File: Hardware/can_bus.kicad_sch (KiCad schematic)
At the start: 4 parts, among them U14 MCP2542FDxMF

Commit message: sync
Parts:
- renumbered C35 to C27, C36 to C28, FB4 to FB3, U14 to U8
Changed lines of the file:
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@@
 (kicad_sch
-	(version 20231120)
+	(version 20250114)
 	(generator "eeschema")
-	(generator_version "8.0")
+	(generator_version "9.0")
 	(paper "A4")
 	(title_block
@@
 		(comment 1 "Reviewer:")
 	)
+	(text "The IC has internal ESD protection"
+		(exclude_from_sim no)
+		(at 147.32 118.11 0)
+		(effects
+			(font
+				(size 1.27 1.27)
+			)
+			(justify left bottom)
+		)
+	)
+	(text "CAN FD compliant transceiver\n"
+		(exclude_from_sim no)
+		(at 147.32 120.65 0)
+		(effects
+			(font
+				(size 1.27 1.27)
+			)
+			(justify left bottom)
+		)
+	)
 	(junction
 		(at 135.89 81.28)
@@
 		)
 	)
-	(text "The IC has internal ESD protection"
-		(exclude_from_sim no)
-		(at 147.32 118.11 0)
+	(hierarchical_label "CAN_H"
+		(shape bidirectional)
+		(at 154.94 102.87 0)
 		(effects
 			(font
 				(size 1.27 1.27)
 			)
-			(justify left bottom)
-		)
-	)
-	(text "CAN FD compliant transceiver\n"
-		(exclude_from_sim no)
-		(at 147.32 120.65 0)
+			(justify left)
+		)
+	)
+	(hierarchical_label "CAN_RX"
+		(shape output)
+		(at 129.54 102.87 180)
 		(effects
 			(font
 				(size 1.27 1.27)
 			)
-			(justify left bottom)
-		)
-	)
-	(hierarchical_label "CAN_H"
+			(justify right)
+		)
+	)
+	(hierarchical_label "CAN_L"
 		(shape bidirectional)
-		(at 154.94 102.87 0)
-		(fields_autoplaced yes)
+		(at 154.94 107.95 0)
 		(effects
 			(font
@@
 		)
 	)
-	(hierarchical_label "CAN_RX"
-		(shape output)
-		(at 129.54 102.87 180)
-		(fields_autoplaced yes)
+	(hierarchical_label "CAN_TX"
+		(shape input)
+		(at 129.54 100.33 180)
 		(effects
 			(font
@@
 		)
 	)
-	(hierarchical_label "CAN_L"
-		(shape bidirectional)
-		(at 154.94 107.95 0)
-		(fields_autoplaced yes)
-		(effects
-			(font
-				(size 1.27 1.27)
-			)
-			(justify left)
-		)
-	)
-	(hierarchical_label "CAN_TX"
-		(shape input)
-		(at 129.54 100.33 180)
-		(fields_autoplaced yes)
-		(effects
-			(font
-				(size 1.27 1.27)
-			)
-			(justify right)
-		)
-	)
 	(symbol
 		(lib_id "Device:C_Small")
@@
 		(dnp no)
 		(fields_autoplaced yes)
-		(property "Reference" "C36"
+		(property "Reference" "C28"
 			(at 148.59 84.4613 0)
 			(effects
@@
 		(on_board yes)
 		(dnp no)
-		(property "Reference" "#PWR0109"
+		(property "Reference" "#PWR061"
 			(at 133.35 95.25 0)
 			(effects
@@
 		(on_board yes)
 		(dnp no)
-		(property "Reference" "#PWR0112"
+		(property "Reference" "#PWR064"
 			(at 142.24 123.19 0)
 			(effects
@@
 		(on_board yes)
 		(dnp no)
-		(property "Reference" "#PWR0108"
+		(property "Reference" "#PWR060"
 			(at 128.27 118.11 0)
 			(effects
@@
 		(dnp no)
 		(fields_autoplaced yes)
-		(property "Reference" "#FLG010"
+		(property "Reference" "#FLG09"
 			(at 160.655 88.9 0)
 			(effects
@@
 		(on_board yes)
 		(dnp no)
-		(property "Reference" "#PWR0113"
+		(property "Reference" "#PWR065"
 			(at 146.05 95.25 0)
 			(effects
@@
 		(on_board yes)
 		(dnp no)
-		(property "Reference" "C35"
+		(property "Reference" "C27"
 			(at 130.81 84.4613 0)
 			(effects
@@
 		(dnp no)
 		(fields_autoplaced yes)
-		(property "Reference" "#PWR0110"
+		(property "Reference" "#PWR062"
 			(at 135.89 83.82 0)
 			(effects
@@
 		(on_board yes)
 		(dnp no)
-		(property "Reference" "U14"
+		(property "Reference" "U8"
 			(at 149.86 114.3 0)
 			(effects
@@
 		(dnp no)
 		(fields_autoplaced yes)
-		(property "Reference" "#PWR0111"
+		(property "Reference" "#PWR063"
 			(at 142.24 78.105 0)
 			(effects
@@
 		(dnp no)
 		(fields_autoplaced yes)
-		(property "Reference" "FB4"
+		(property "Reference" "FB3"
 			(at 144.78 76.7969 0)
 			(effects

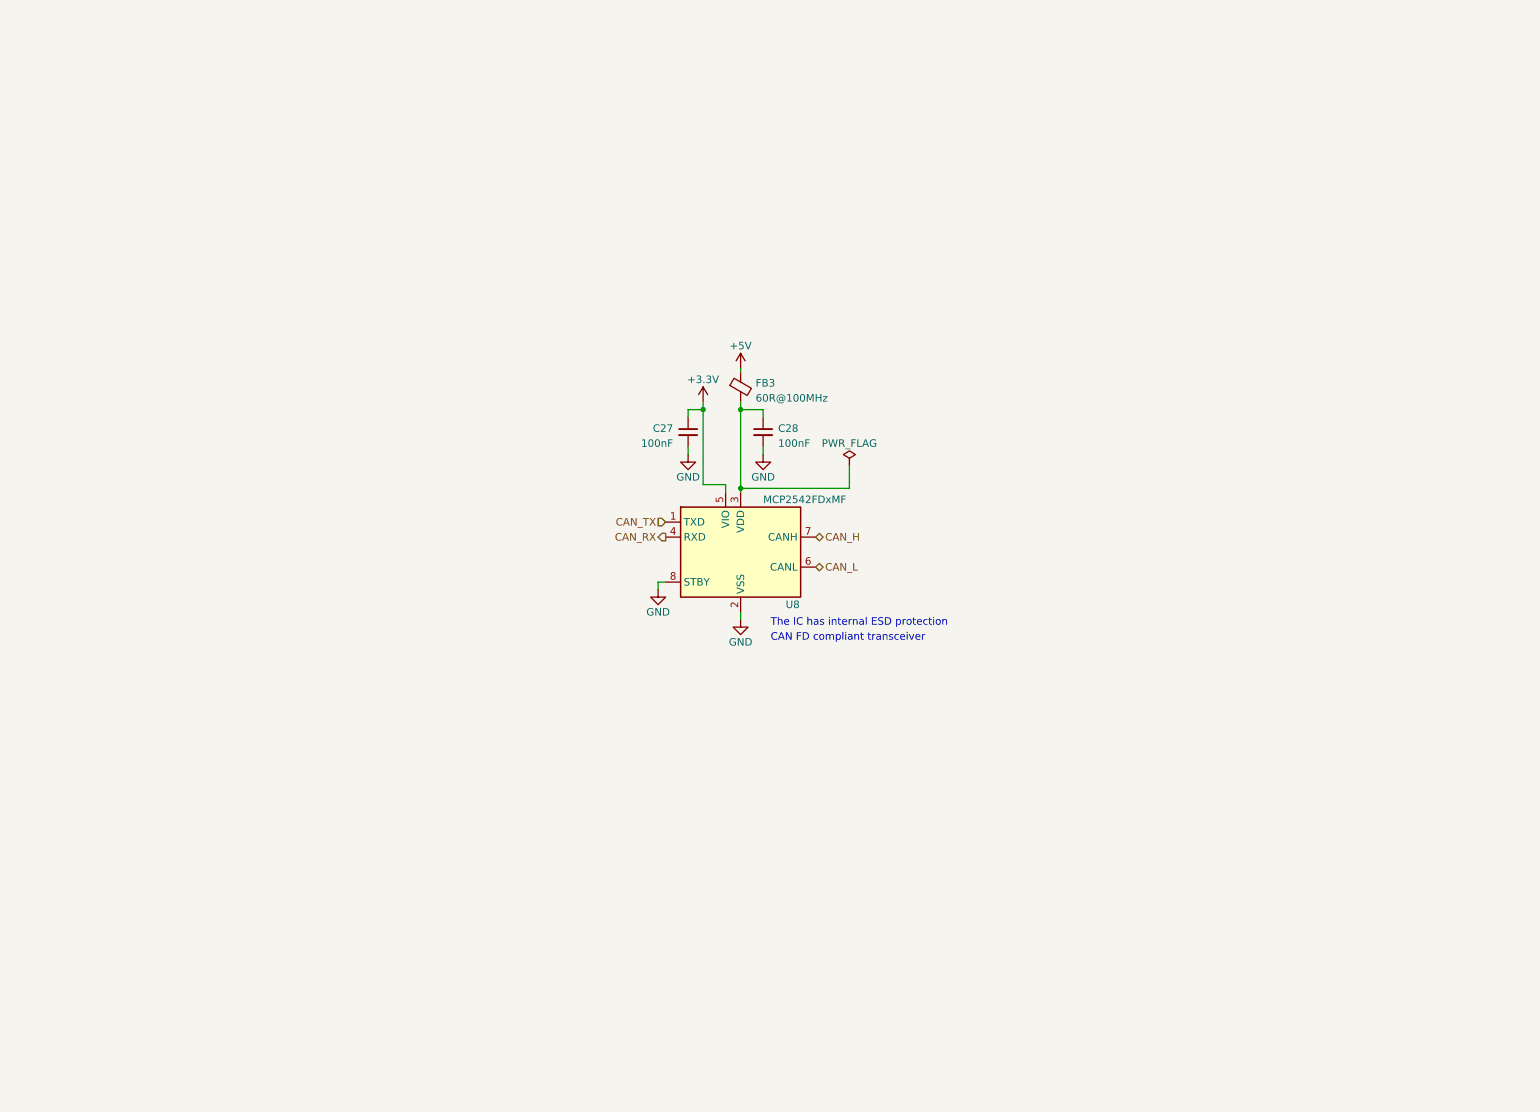
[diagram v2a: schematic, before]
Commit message: Created new hardware version 2.0
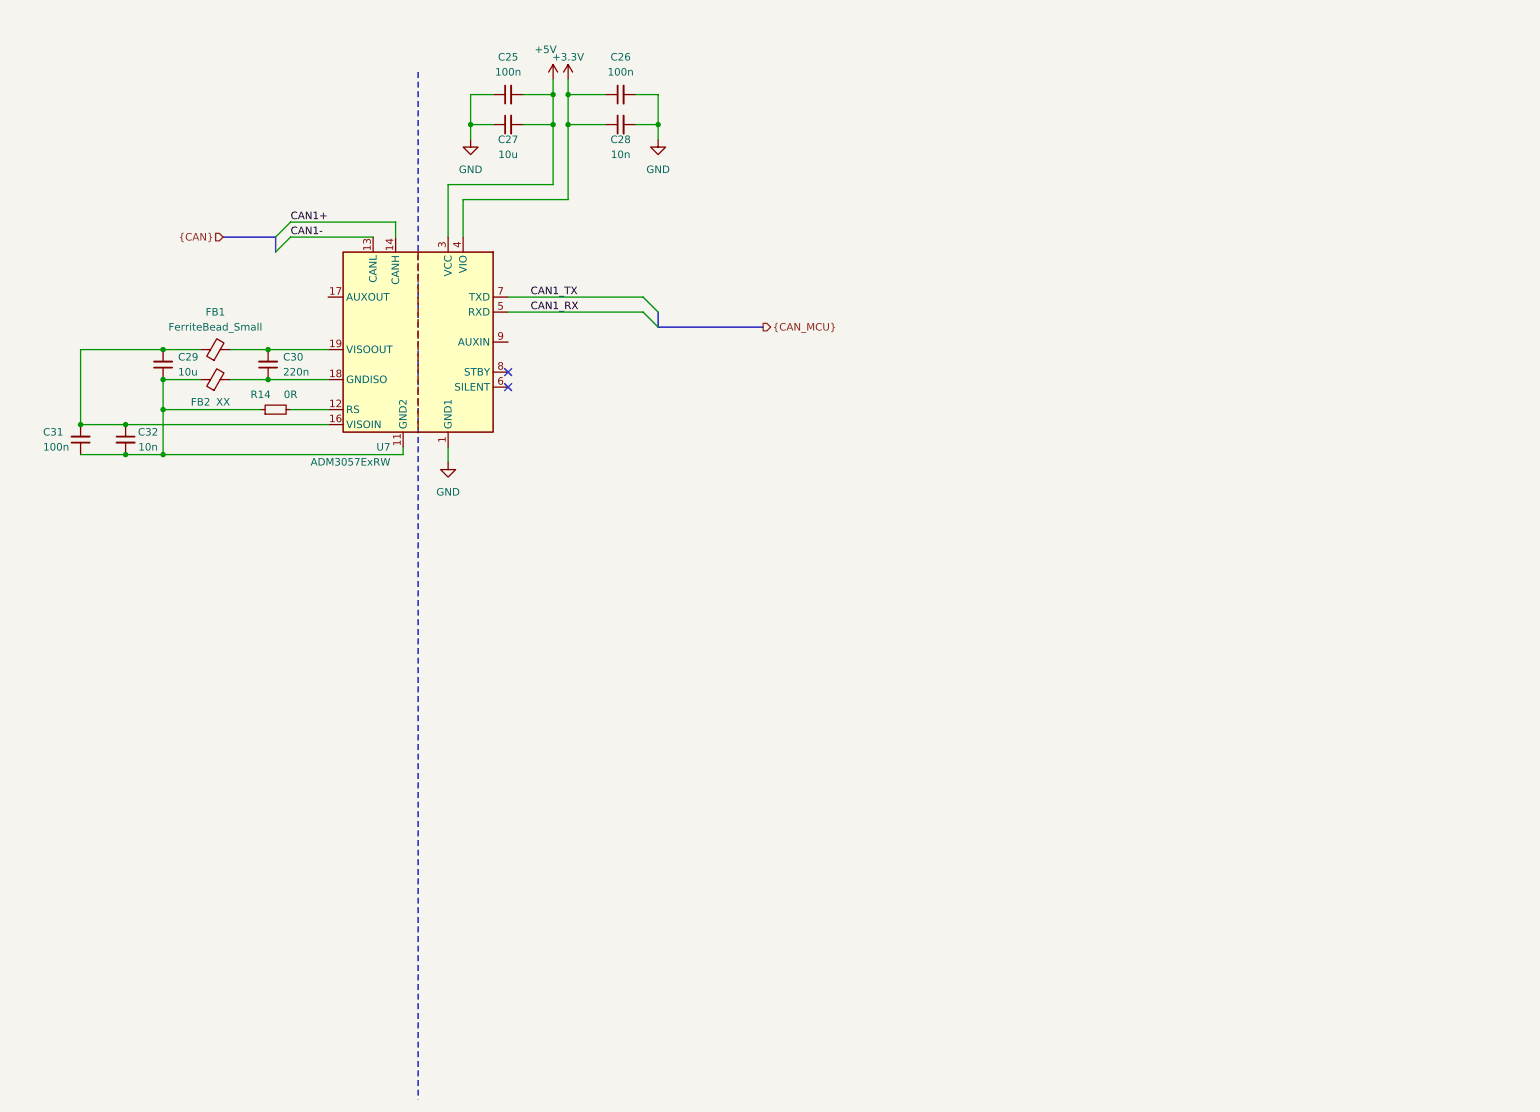
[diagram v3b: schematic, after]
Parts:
- removed FB3: 60R@100MHz, Inductor_SMD:L_0603_1608Metric, symbol Device:FerriteBead_Small
- removed U8: MCP2542FDxMF, Package_DFN_QFN:DFN-8-1EP_3x3mm_P0.65mm_EP1.55x2.4mm, symbol Interface_CAN_LIN:MCP2542FDxMF
- added C25, C26, C31: 100n, Capacitor_SMD:C_0603_1608Metric_Pad1.08x0.95mm_HandSolder, symbol Device:C_Small
- added C29: 10u, Capacitor_SMD:C_0603_1608Metric_Pad1.08x0.95mm_HandSolder, symbol Device:C_Small
- added C30: 220n, Capacitor_SMD:C_0603_1608Metric_Pad1.08x0.95mm_HandSolder, symbol Device:C_Small
- added C32: 10n, Capacitor_SMD:C_0603_1608Metric_Pad1.08x0.95mm_HandSolder, symbol Device:C_Small
- added FB1: FerriteBead_Small, symbol Device:FerriteBead_Small
- added FB2: XX, symbol Device:FerriteBead_Small
- added R14: 0R, Resistor_SMD:R_0603_1608Metric_Pad0.98x0.95mm_HandSolder, symbol Device:R_Small
- added U7: ADM3057ExRW, Package_SO:SOIC-20W_7.5x12.8mm_P1.27mm, symbol Interface_CAN_LIN:ADM3057ExRW
- C27: value 100nF -> 10u; footprint Capacitor_SMD:C_0402_1005Metric_Pad0.74x0.62mm_HandSolder -> Capacitor_SMD:C_0603_1608Metric_Pad1.08x0.95mm_HandSolder
- C28: value 100nF -> 10n; footprint Capacitor_SMD:C_0402_1005Metric_Pad0.74x0.62mm_HandSolder -> Capacitor_SMD:C_0603_1608Metric_Pad1.08x0.95mm_HandSolder
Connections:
- net +3.3V: now also C28.1, C26.1, U7.4 (VIO); no longer C27.1
- net +5V: now also C27.2, C25.2, U7.3 (VCC)
- net GND: now also C27.1, C25.1, C26.2, U7.1 (GND1), U7.10 (GND1), U7.2 (GND1); no longer C27.2
- new net: C29.1, C31.1, C32.2, FB2.1, R14.1, U7.11 (GND2), U7.15 (GND2)
- new net: C30.1, FB2.2, U7.18 (GNDISO), U7.20 (GNDISO)
- new net: R14.2, U7.12 (RS)
- new net: C29.2, C31.2, C32.1, FB1.1, U7.16 (VISOIN)
- new net: C30.2, FB1.2, U7.19 (VISOOUT)
- new net CAN1+: U7.14 (CANH)
- new net CAN1-: U7.13 (CANL)
- new net CAN1_RX: U7.5 (RXD)
- new net CAN1_TX: U7.7 (TXD)
- no-connect marks 0 -> 2
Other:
- note removed: "CAN FD compliant transceiver"
- note removed: "The IC has internal ESD protection"
- company: Author: Szymon Kostrubiec -> (none)
- title: CAN bus -> (none)

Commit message: Changes in CAN section
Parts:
- added C53, C57, C59: 100n, Capacitor_SMD:C_0603_1608Metric_Pad1.08x0.95mm_HandSolder, symbol Device:C_Small
- added C54, C60: 10n, Capacitor_SMD:C_0603_1608Metric_Pad1.08x0.95mm_HandSolder, symbol Device:C_Small
- added C55, C58: 47u, Capacitor_SMD:C_0603_1608Metric_Pad1.08x0.95mm_HandSolder, symbol Device:C_Small
- added C56: 220n, Capacitor_SMD:C_0603_1608Metric_Pad1.08x0.95mm_HandSolder, symbol Device:C_Small
- added FB3, FB4, FB5, FB6, FB7, FB8: 2K@100MHz, Inductor_SMD:L_0603_1608Metric_Pad1.05x0.95mm_HandSolder, symbol Device:FerriteBead_Small
- added R51: 0R, Resistor_SMD:R_0603_1608Metric_Pad0.98x0.95mm_HandSolder, symbol Device:R_Small
- added U14: ADM3057ExRW, Package_SO:SOIC-20W_7.5x12.8mm_P1.27mm, symbol Interface_CAN_LIN:ADM3057ExRW
- C27, C29: value 10u -> 47u
- FB1: value FerriteBead_Small -> 2K@100MHz; footprint (none) -> Inductor_SMD:L_0603_1608Metric_Pad1.05x0.95mm_HandSolder
- FB2: value XX -> 2K@100MHz; footprint (none) -> Inductor_SMD:L_0603_1608Metric_Pad1.05x0.95mm_HandSolder
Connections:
- net +3.3V: now also C59.1, FB4.2, FB8.2; no longer C28.1, U7.4 (VIO)
- net +5V: now also C57.2, FB3.2, FB7.2; no longer C27.2, U7.3 (VCC)
- net GND: now also U7.9 (AUXIN), C57.1, C58.1, C59.2, C60.2, U14.1 (GND1), U14.10 (GND1), U14.2 (GND1), U14.9 (AUXIN)
- net GND_CAN_ISO: now reaches C29.1, C31.1, C32.2, FB2.1, R14.1, U7.11 (GND2), U7.15 (GND2)
- net GND_CAN_ISO: now also C53.1, C54.2, C55.1, FB6.1, R51.1, U14.11 (GND2), U14.15 (GND2)
- net STBY_CAN_1: now reaches U7.8 (STBY)
- new net: C58.2, FB7.1, U14.3 (VCC)
- new net: C27.2, FB3.1, U7.3 (VCC)
- new net: R51.2, U14.12 (RS)
- new net: C53.2, C54.1, C55.2, FB5.1, U14.16 (VISOIN)
- new net: C56.1, FB6.2, U14.18 (GNDISO), U14.20 (GNDISO)
- new net: C56.2, FB5.2, U14.19 (VISOOUT)
- new net: C60.1, FB8.1, U14.4 (VIO)
- new net: C28.1, FB4.1, U7.4 (VIO)
- new net CAN2+: U14.14 (CANH)
- new net CAN2-: U14.13 (CANL)
- new net CAN2_RX: U14.5 (RXD)
- new net CAN2_TX: U14.7 (TXD)
- new net STBY_CAN_2: U14.8 (STBY)
- no-connect marks 2 -> 4
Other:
- moved on the sheet: C25, C26, C27, C28

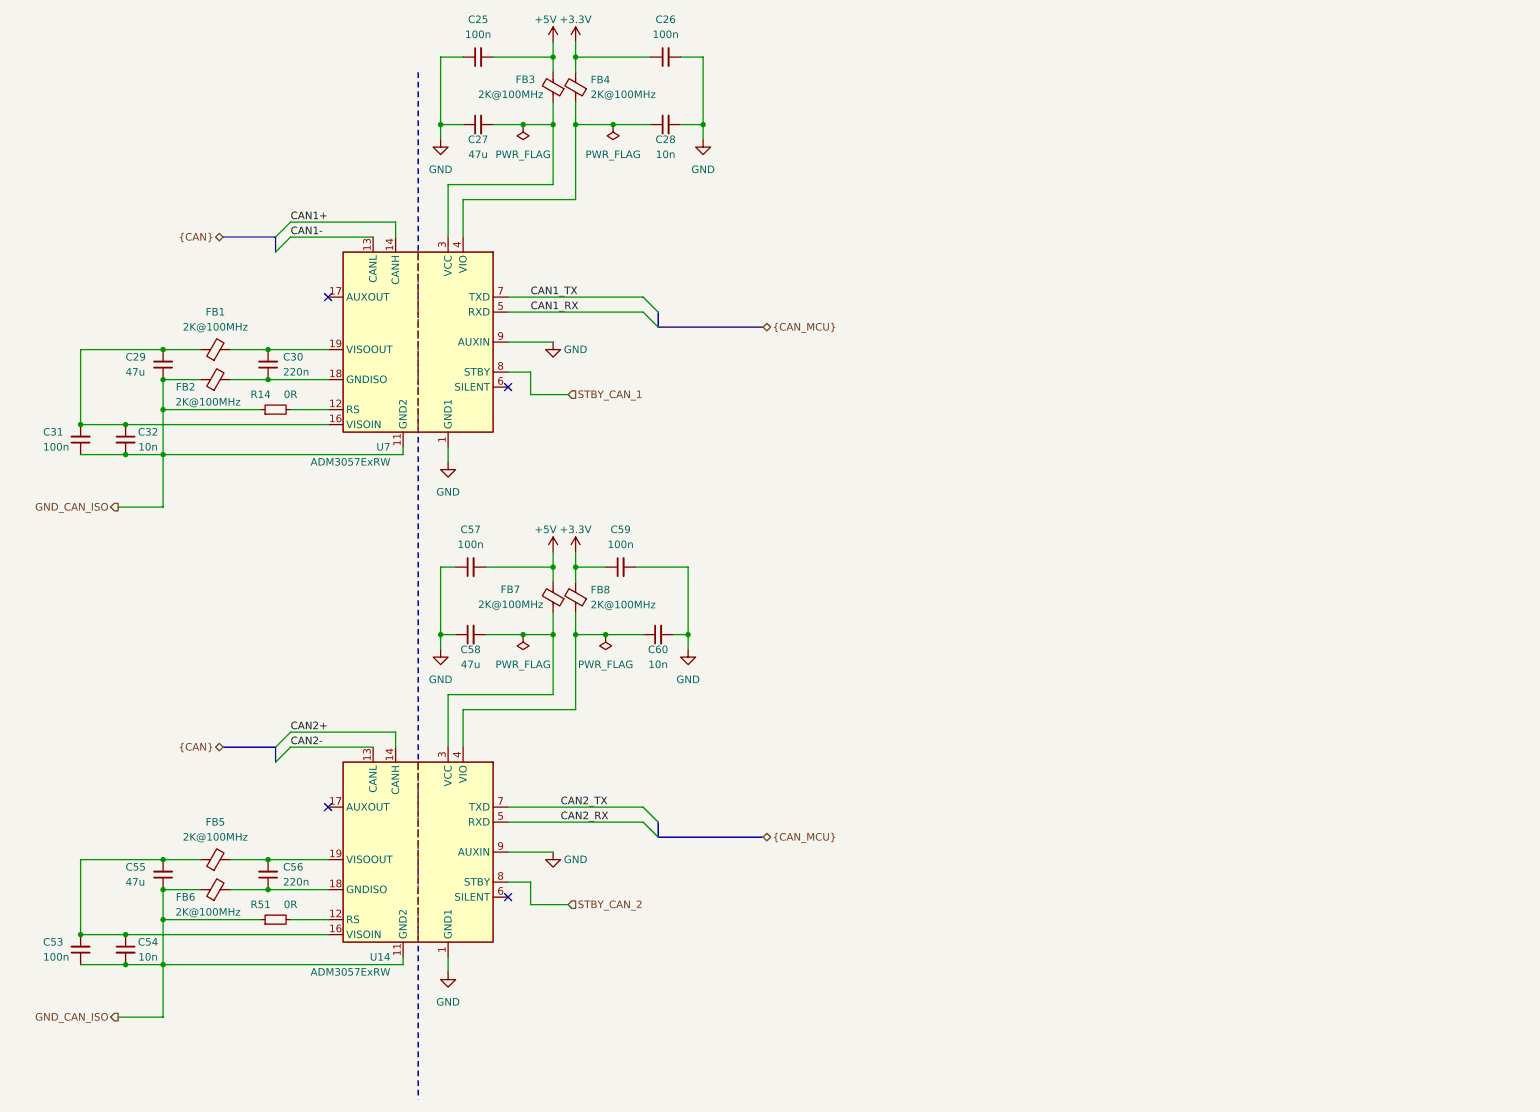
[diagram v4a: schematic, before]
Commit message: Changes in schematic, separated CAN buses, added XIAO Sense S3 DevBoard
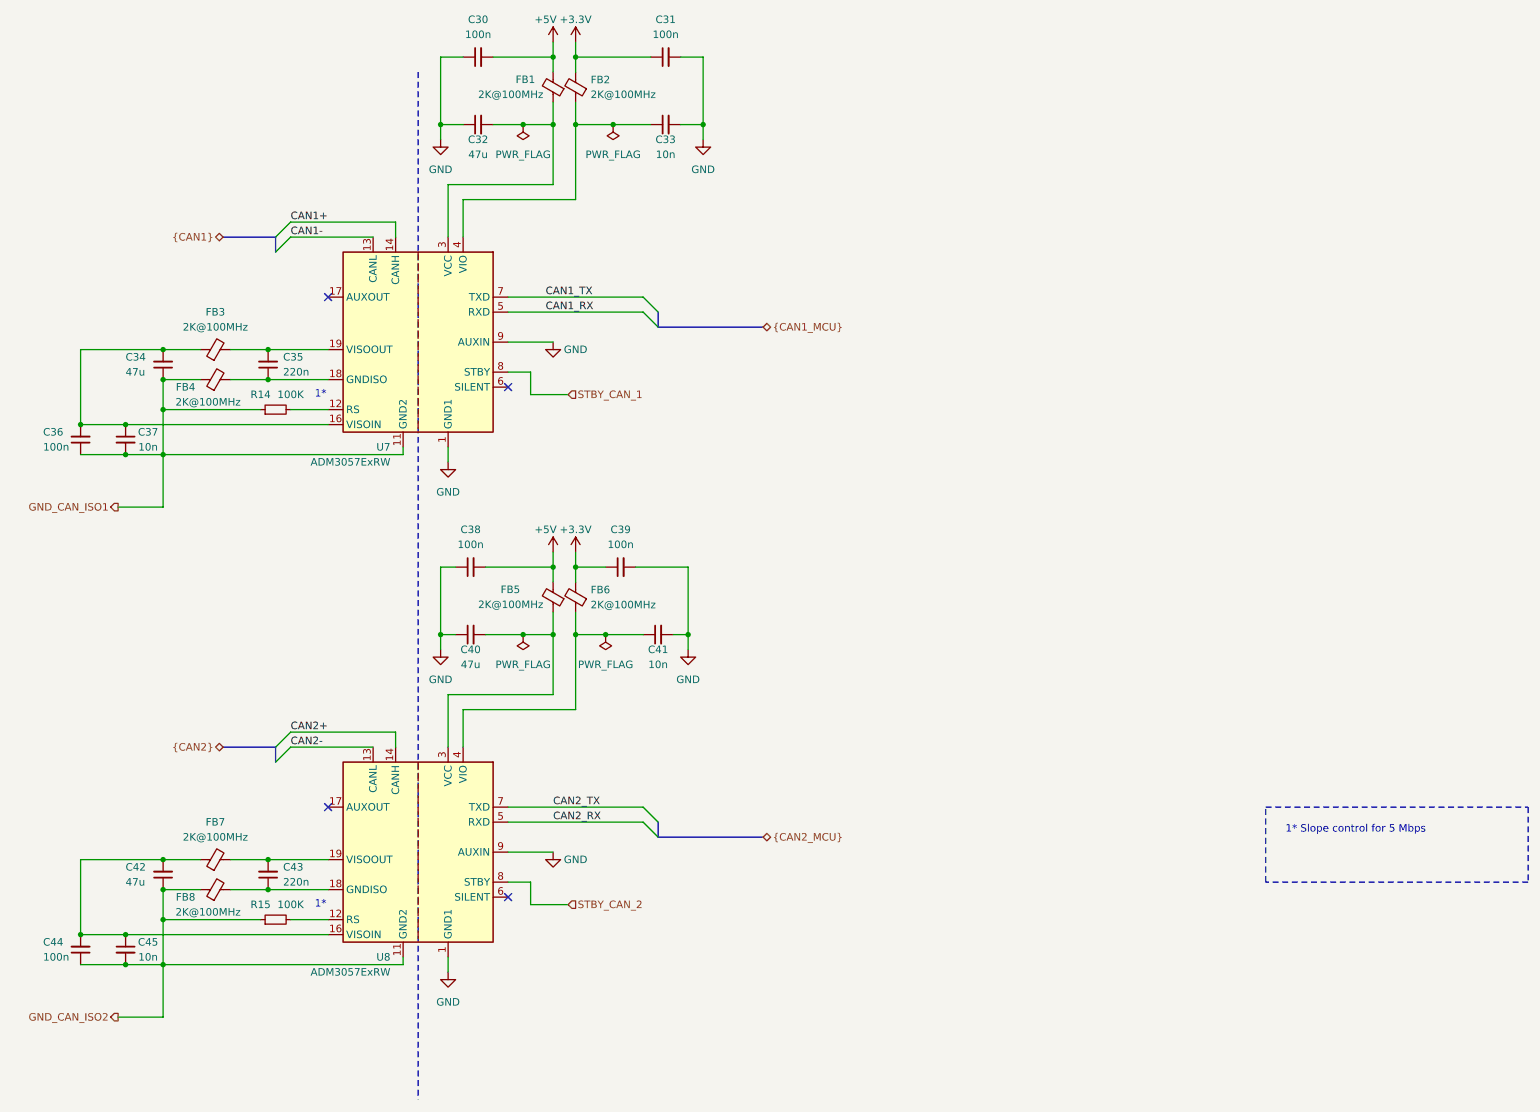
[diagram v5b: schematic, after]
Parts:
- R14: value 0R -> 100K
- R15: renamed from R51; value 0R -> 100K
- renumbered C25 to C30, C26 to C31, C27 to C32, C28 to C33, C29 to C34, C30 to C35, C31 to C36, C32 to C37, C57 to C38, C59 to C39, C58 to C40, C60 to C41, C55 to C42, C56 to C43, C53 to C44, C54 to C45, FB3 to FB1, FB4 to FB2, FB1 to FB3, FB2 to FB4, FB7 to FB5, FB8 to FB6, FB5 to FB7, FB6 to FB8, U14 to U8
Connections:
- net GND_CAN_ISO renamed GND_CAN_ISO1
- net GND_CAN_ISO1: no longer C42.1, C44.1, C45.2, FB8.1, R15.1, U8.11 (GND2), U8.15 (GND2)
- new net GND_CAN_ISO2: C42.1, C44.1, C45.2, FB8.1, R15.1, U8.11 (GND2), U8.15 (GND2)
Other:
- note added: "1*"
- note added: "1* Slope control for 5 Mbps"
